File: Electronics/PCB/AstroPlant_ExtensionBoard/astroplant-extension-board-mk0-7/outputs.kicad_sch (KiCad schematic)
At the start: 17 parts, among them J12 JST-XH_LED_GND, J13 GS3, J14 GS3, J15 GS3, J16 JST_HX_2, J17 JST_HX_2, J18 JST_HX_2, J19 JST_HX_2, Q3 IRLML6344TRPBF, Q4 IRLML6344TRPBF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

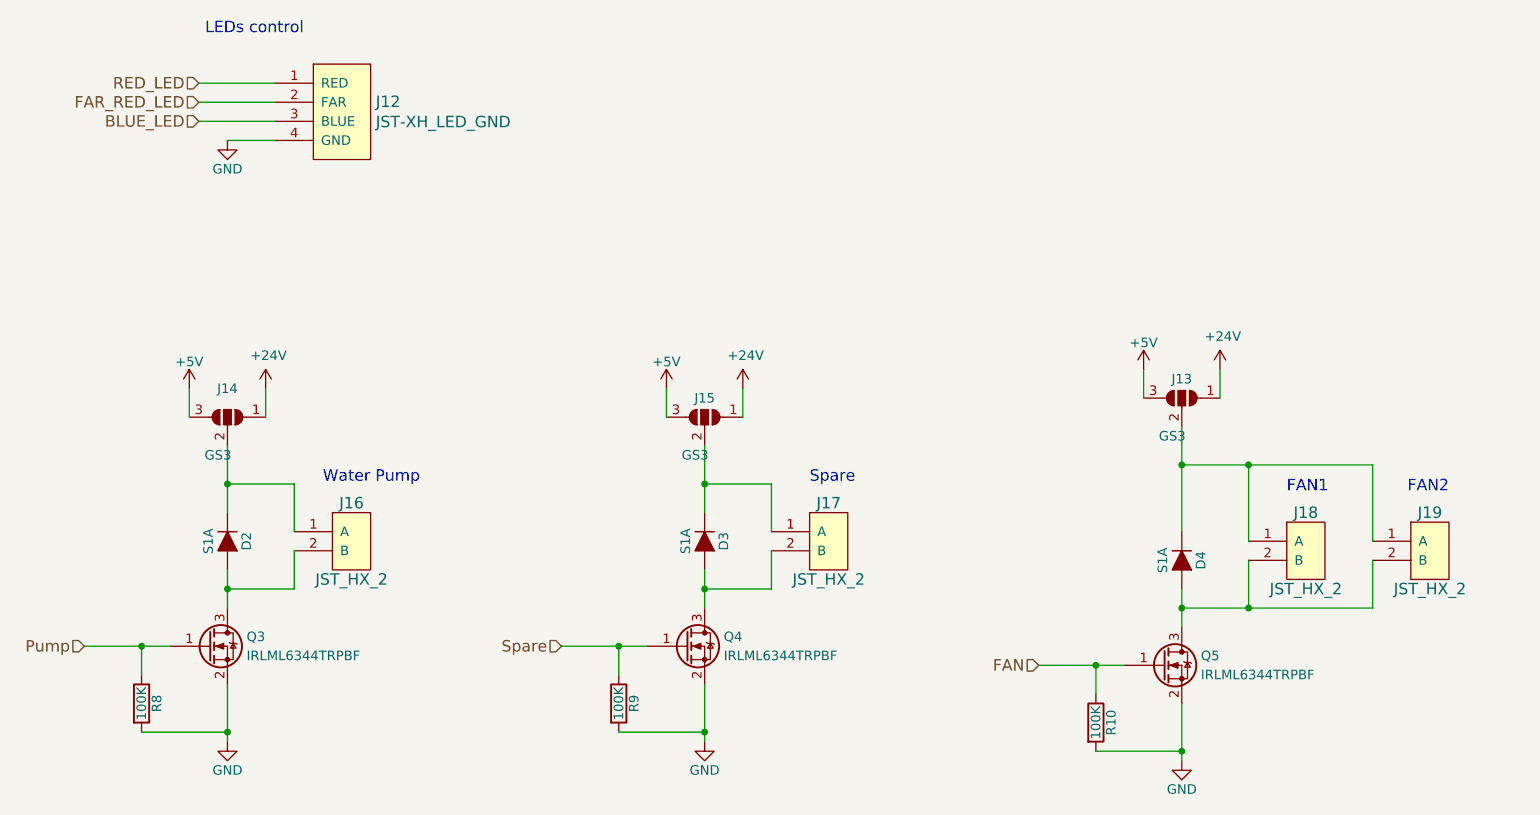
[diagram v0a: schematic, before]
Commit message: Update schematic and change library path
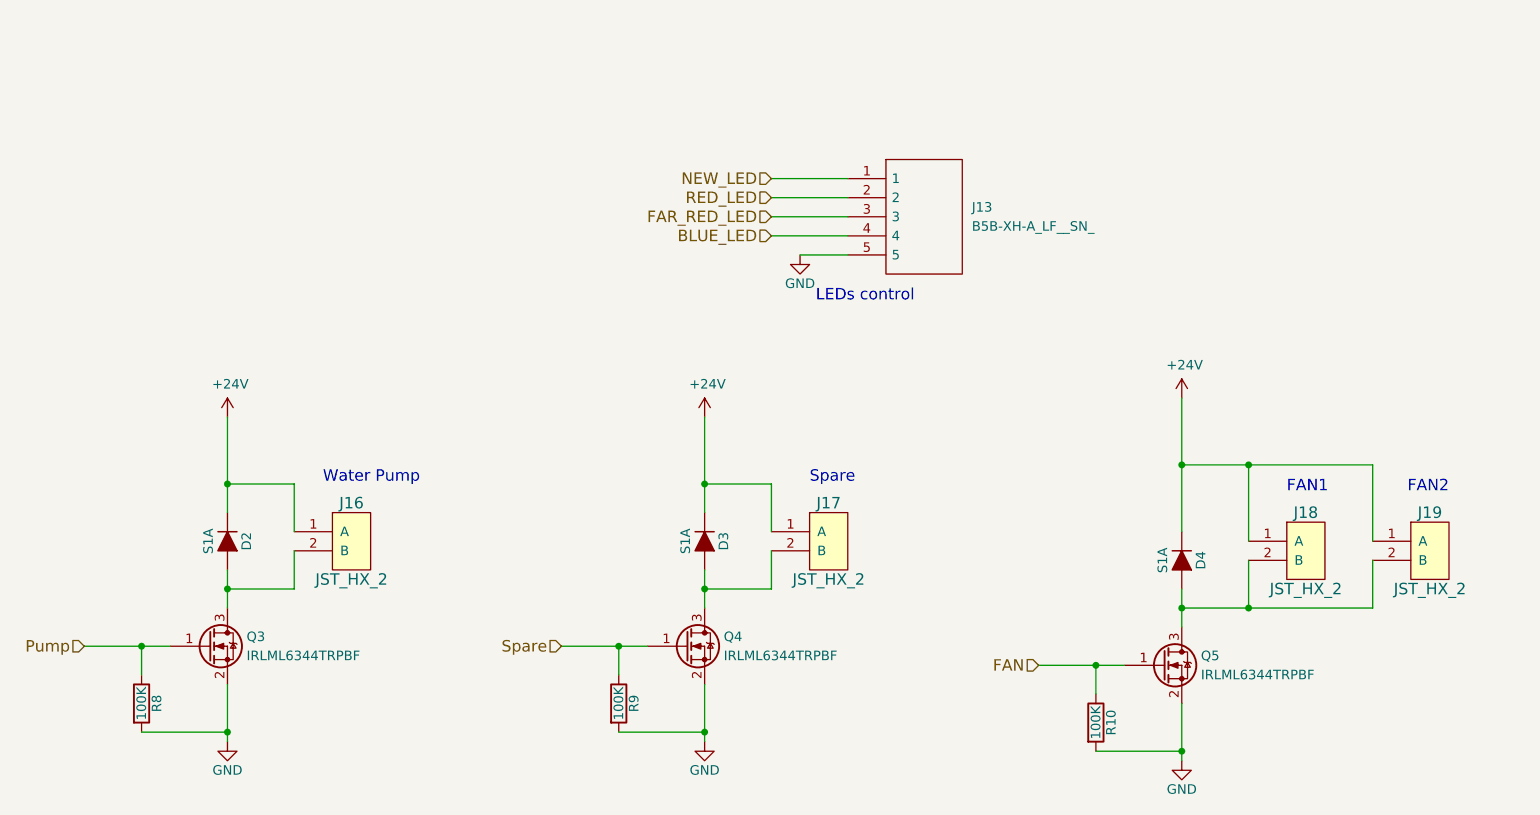
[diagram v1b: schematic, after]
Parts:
- removed J12: JST-XH_LED_GND, Connector_JST:JST_XH_B04B-XH-A_1x04_P2.50mm_Vertical, symbol Astroplant_VFR-rescue:JST-XH_LED_GND-JST_connector
- removed J13, J14, J15: GS3, Jumper:SolderJumper-3_P2.0mm_Open_TrianglePad1.0x1.5mm, symbol Astroplant_VFR-rescue:SolderJumper_3_Open-Jumper
- added J13: B5B-XH-A_LF__SN_, SHDR5W64P0X250_1X5_1490X575X700P, symbol SamacSys_Parts:B5B-XH-A_LF__SN_
- J16, J17, J18, J19: footprint Connector_JST:JST_XH_B02B-XH-A_1x02_P2.50mm_Vertical -> SamacSys_Parts:SHDR2W64P0X250_1X2_740X575X700P
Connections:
- net +24V: now also D2.1 (K), D3.1 (K), D4.1 (K), J16.1 (A), J17.1 (A), J18.1 (A), J19.1 (A)
- net BLUE_LED: now also J13.4
- net FAR_RED_LED: now also J13.3
- net GND: now also J13.5
- net RED_LED: now also J13.2
- new net NEW_LED: J13.1

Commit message: Place components on PCB
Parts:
- removed R10, R8, R9: 100K, Resistor_SMD:R_0805_2012Metric, symbol Device:R
- added R24, R25 (x2): 10k, Resistor_SMD:R_0603_1608Metric, symbol Device:R_Small
- J13: footprint SHDR5W64P0X250_1X5_1490X575X700P -> SamacSys_Parts:SHDR5W64P0X250_1X5_1490X575X700P
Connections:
- net FAN: now also R25.2
- net GND: now also R24.1, R25.1, R25.1
- net Pump: now also R24.2
- net Spare: now also R25.2
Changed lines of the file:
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@@
+    (stroke (width 0) (type default))
+  )
+  (wire (pts (xy 121.92 135.89) (xy 121.92 138.43))
     (stroke (width 0) (type default))
   )
@@
     (stroke (width 0) (type default))
   )
+  (wire (pts (xy 58.42 135.89) (xy 58.42 138.43))
+    (stroke (width 0) (type default))
+  )
   (wire (pts (xy 69.85 96.52) (xy 69.85 105.41))
     (stroke (width 0) (type default))
@@
   )
   (wire (pts (xy 205.74 113.03) (xy 205.74 102.87))
+    (stroke (width 0) (type default))
+  )
+  (wire (pts (xy 185.42 138.43) (xy 185.42 140.97))
     (stroke (width 0) (type default))
   )
@@
         (path "/51acab52-3cd6-4bba-9dee-c12efd332038/00000000-0000-0000-0000-00005a604cdc"
           (reference "D4") (unit 1)
-        )
-      )
-    )
-  )
-  (symbol (lib_id "Device:R") (at 58.42 134.62 0) (unit 1)
-    (in_bom yes) (on_board yes) (dnp no)
-    (property "Reference" "R8" (at 60.452 134.62 90)
-      (effects (font (size 1.27 1.27)))
-    )
-    (property "Value" "100K" (at 58.42 134.62 90)
-      (effects (font (size 1.27 1.27)))
-    )
-    (property "Footprint" "Resistor_SMD:R_0805_2012Metric" (at 56.642 134.62 90)
-      (effects (font (size 1.27 1.27)) hide)
-    )
-    (property "Datasheet" "http://www.yageo.com/documents/recent/PYu-RC_Group_51_RoHS_L_8.pdf" (at 58.42 134.62 0)
-      (effects (font (size 1.27 1.27)) hide)
-    )
-    (property "MPN" "RC0805FR-07100KL " (at 58.42 134.62 0)
-      (effects (font (size 1.524 1.524)) hide)
-    )
-    (property "URL" "https://www.digikey.com/product-detail/en/yageo/RC0805FR-07100KL/311-100KCRCT-ND/730491" (at 58.42 134.62 0)
-      (effects (font (size 1.524 1.524)) hide)
-    )
-    (property "Digikey Part Number" "311-100KCRCT-ND" (at 58.42 134.62 0)
-      (effects (font (size 1.524 1.524)) hide)
-    )
-    (pin "1")
-    (pin "2")
-    (instances
-      (project "Astroplant_VFR"
-        (path "/4e818498-015c-45b7-982b-80c19490efdc/00000000-0000-0000-0000-00005a604cdc"
-          (reference "R8") (unit 1)
-        )
-      )
-      (project "Astroplant_AL"
-        (path "/51acab52-3cd6-4bba-9dee-c12efd332038/00000000-0000-0000-0000-00005a604cdc"
-          (reference "R8") (unit 1)
-        )
-      )
-    )
-  )
-  (symbol (lib_id "Device:R") (at 185.42 137.16 0) (unit 1)
-    (in_bom yes) (on_board yes) (dnp no)
-    (property "Reference" "R10" (at 187.452 137.16 90)
-      (effects (font (size 1.27 1.27)))
-    )
-    (property "Value" "100K" (at 185.42 137.16 90)
-      (effects (font (size 1.27 1.27)))
-    )
-    (property "Footprint" "Resistor_SMD:R_0805_2012Metric" (at 183.642 137.16 90)
-      (effects (font (size 1.27 1.27)) hide)
-    )
-    (property "Datasheet" "http://www.yageo.com/documents/recent/PYu-RC_Group_51_RoHS_L_8.pdf" (at 185.42 137.16 0)
-      (effects (font (size 1.27 1.27)) hide)
-    )
-    (property "MPN" "RC0805FR-07100KL " (at 185.42 137.16 0)
-      (effects (font (size 1.524 1.524)) hide)
-    )
-    (property "URL" "https://www.digikey.com/product-detail/en/yageo/RC0805FR-07100KL/311-100KCRCT-ND/730491" (at 185.42 137.16 0)
-      (effects (font (size 1.524 1.524)) hide)
-    )
-    (property "Digikey Part Number" "311-100KCRCT-ND" (at 185.42 137.16 0)
-      (effects (font (size 1.524 1.524)) hide)
-    )
-    (pin "1")
-    (pin "2")
-    (instances
-      (project "Astroplant_VFR"
-        (path "/4e818498-015c-45b7-982b-80c19490efdc/00000000-0000-0000-0000-00005a604cdc"
-          (reference "R10") (unit 1)
-        )
-      )
-      (project "Astroplant_AL"
-        (path "/51acab52-3cd6-4bba-9dee-c12efd332038/00000000-0000-0000-0000-00005a604cdc"
-          (reference "R10") (unit 1)
-        )
-      )
-    )
-  )
-  (symbol (lib_id "Device:R") (at 121.92 134.62 0) (unit 1)
-    (in_bom yes) (on_board yes) (dnp no)
-    (property "Reference" "R9" (at 123.952 134.62 90)
-      (effects (font (size 1.27 1.27)))
-    )
-    (property "Value" "100K" (at 121.92 134.62 90)
-      (effects (font (size 1.27 1.27)))
-    )
-    (property "Footprint" "Resistor_SMD:R_0805_2012Metric" (at 120.142 134.62 90)
-      (effects (font (size 1.27 1.27)) hide)
-    )
-    (property "Datasheet" "http://www.yageo.com/documents/recent/PYu-RC_Group_51_RoHS_L_8.pdf" (at 121.92 134.62 0)
-      (effects (font (size 1.27 1.27)) hide)
-    )
-    (property "MPN" "RC0805FR-07100KL " (at 121.92 134.62 0)
-      (effects (font (size 1.524 1.524)) hide)
-    )
-    (property "URL" "https://www.digikey.com/product-detail/en/yageo/RC0805FR-07100KL/311-100KCRCT-ND/730491" (at 121.92 134.62 0)
-      (effects (font (size 1.524 1.524)) hide)
-    )
-    (property "Digikey Part Number" "311-100KCRCT-ND" (at 121.92 134.62 0)
-      (effects (font (size 1.524 1.524)) hide)
-    )
-    (pin "1")
-    (pin "2")
-    (instances
-      (project "Astroplant_VFR"
-        (path "/4e818498-015c-45b7-982b-80c19490efdc/00000000-0000-0000-0000-00005a604cdc"
-          (reference "R9") (unit 1)
-        )
-      )
-      (project "Astroplant_AL"
-        (path "/51acab52-3cd6-4bba-9dee-c12efd332038/00000000-0000-0000-0000-00005a604cdc"
-          (reference "R9") (unit 1)
         )
       )
@@
       (effects (font (size 1.27 1.27)) (justify left))
     )
-    (property "Footprint" "SHDR5W64P0X250_1X5_1490X575X700P" (at 168.91 62.23 0)
+    (property "Footprint" "SamacSys_Parts:SHDR5W64P0X250_1X5_1490X575X700P" (at 168.91 62.23 0)
       (effects (font (size 1.27 1.27)) (justify left) hide)
     )
@@
     )
   )
+  (symbol (lib_id "Device:R_Small") (at 185.42 135.89 180) (unit 1)
+    (in_bom yes) (on_board yes) (dnp no) (fields_autoplaced)
+    (property "Reference" "R25" (at 187.96 134.62 0)
+      (effects (font (size 1.27 1.27)) (justify right))
+    )
+    (property "Value" "10k" (at 187.96 137.16 0)
+      (effects (font (size 1.27 1.27)) (justify right))
+    )
+    (property "Footprint" "Resistor_SMD:R_0603_1608Metric" (at 185.42 135.89 0)
+      (effects (font (size 1.27 1.27)) hide)
+    )
+    (property "Datasheet" "~" (at 185.42 135.89 0)
+      (effects (font (size 1.27 1.27)) hide)
+    )
+    (property "MPN" "CRCW060310K0DHEAP" (at 185.42 135.89 0)
+      (effects (font (size 1.27 1.27)) hide)
+    )
+    (pin "1")
+    (pin "2")
+    (instances
+      (project "Astroplant_AL"
+        (path "/51acab52-3cd6-4bba-9dee-c12efd332038/5f0c961f-7fa6-4a15-8a74-755a432cc19e"
+          (reference "R25") (unit 1)
+        )
+        (path "/51acab52-3cd6-4bba-9dee-c12efd332038/00000000-0000-0000-0000-00005a604cdc"
+          (reference "R10") (unit 1)
+        )
+      )
+    )
+  )
   (symbol (lib_id "power:GND") (at 146.05 74.93 0) (unit 1)
     (in_bom yes) (on_board yes) (dnp no)
@@
         )
       )
+    )
+  )
+  (symbol (lib_id "Device:R_Small") (at 121.92 133.35 180) (unit 1)
+    (in_bom yes) (on_board yes) (dnp no) (fields_autoplaced)
+    (property "Reference" "R25" (at 124.46 132.08 0)
+      (effects (font (size 1.27 1.27)) (justify right))
+    )
+    (property "Value" "10k" (at 124.46 134.62 0)
+      (effects (font (size 1.27 1.27)) (justify right))
+    )
+    (property "Footprint" "Resistor_SMD:R_0603_1608Metric" (at 121.92 133.35 0)
+      (effects (font (size 1.27 1.27)) hide)
+    )
+    (property "Datasheet" "~" (at 121.92 133.35 0)
+      (effects (font (size 1.27 1.27)) hide)
+    )
+    (property "MPN" "CRCW060310K0DHEAP" (at 121.92 133.35 0)
+      (effects (font (size 1.27 1.27)) hide)
+    )
+    (pin "1")
+    (pin "2")
+    (instances
+      (project "Astroplant_AL"
+        (path "/51acab52-3cd6-4bba-9dee-c12efd332038/5f0c961f-7fa6-4a15-8a74-755a432cc19e"
+          (reference "R25") (unit 1)
+        )
+        (path "/51acab52-3cd6-4bba-9dee-c12efd332038/00000000-0000-0000-0000-00005a604cdc"
+          (reference "R9") (unit 1)
+        )
+      )
+    )
+  )
+  (symbol (lib_id "Device:R_Small") (at 58.42 133.35 180) (unit 1)
+    (in_bom yes) (on_board yes) (dnp no) (fields_autoplaced)
+    (property "Reference" "R24" (at 60.96 132.08 0)
+      (effects (font (size 1.27 1.27)) (justify right))
+    )
+    (property "Value" "10k" (at 60.96 134.62 0)
+      (effects (font (size 1.27 1.27)) (justify right))
+    )
+    (property "Footprint" "Resistor_SMD:R_0603_1608Metric" (at 58.42 133.35 0)
+      (effects (font (size 1.27 1.27)) hide)
+    )
+    (property "Datasheet" "~" (at 58.42 133.35 0)
+      (effects (font (size 1.27 1.27)) hide)
+    )
+    (property "MPN" "CRCW060310K0DHEAP" (at 58.42 133.35 0)
+      (effects (font (size 1.27 1.27)) hide)
+    )
+    (pin "1")
+    (pin "2")
+    (instances
+      (project "Astroplant_AL"
+        (path "/51acab52-3cd6-4bba-9dee-c12efd332038/5f0c961f-7fa6-4a15-8a74-755a432cc19e"
+          (reference "R24") (unit 1)
+        )
+        (path "/51acab52-3cd6-4bba-9dee-c12efd332038/00000000-0000-0000-0000-00005a604cdc"
+          (reference "R8") (unit 1)
+        )
+      )

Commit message: Completed version of the project
Generate outputs (BOM, Drill, Pkp, Gerber)
Added connectors descritption (like "I2C 3.3V" dor the corresponding connector)
Added a connector to an external antenna
Changed routing
Changed component placement
Added a script to generate a usable BOM
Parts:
- J13: MPN (none) -> B5B-XH-A(LF)(SN)
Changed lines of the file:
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@@
       (effects (font (size 1.27 1.27)) (justify left) hide)
+    )
+    (property "MPN" "B5B-XH-A(LF)(SN)" (at 152.4 64.77 0)
+      (effects (font (size 1.27 1.27)) hide)
     )
     (pin "1")

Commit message: Updated PCB from a backup save to solve issue with git
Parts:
- D2, D3, D4: value S1A -> S1A-13-F
- J13: value B5B-XH-A_LF__SN_ -> B5B-XH-A(LF)(SN)
- J16, J17, J18, J19: value JST_HX_2 -> B2B-XH-A(LF)(SN)
- R24, R25: value 10k -> CRCW060310K0DHEAP
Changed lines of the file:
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@@
       (effects (font (size 1.27 1.27)))
     )
-    (property "Value" "S1A" (at 67.31 113.03 0)
+    (property "Value" "S1A-13-F" (at 67.31 113.03 0)
       (effects (font (size 1.27 1.27)))
     )
@@
       (effects (font (size 1.27 1.27)))
     )
-    (property "Value" "S1A" (at 130.81 113.03 0)
+    (property "Value" "S1A-13-F" (at 130.81 113.03 0)
       (effects (font (size 1.27 1.27)))
     )
@@
       (effects (font (size 1.27 1.27)))
     )
-    (property "Value" "S1A" (at 194.31 115.57 0)
+    (property "Value" "S1A-13-F" (at 194.31 115.57 0)
       (effects (font (size 1.27 1.27)))
     )
@@
       (effects (font (size 1.524 1.524)))
     )
-    (property "Value" "JST_HX_2" (at 213.36 119.38 0)
+    (property "Value" "B2B-XH-A(LF)(SN) " (at 213.36 119.38 0)
       (effects (font (size 1.524 1.524)))
     )
@@
       (effects (font (size 1.524 1.524)))
     )
-    (property "Value" "JST_HX_2" (at 229.87 119.38 0)
+    (property "Value" "B2B-XH-A(LF)(SN) " (at 229.87 119.38 0)
       (effects (font (size 1.524 1.524)))
     )
@@
       (effects (font (size 1.524 1.524)))
     )
-    (property "Value" "JST_HX_2" (at 149.86 118.11 0)
+    (property "Value" "B2B-XH-A(LF)(SN) " (at 149.86 118.11 0)
       (effects (font (size 1.524 1.524)))
     )
@@
       (effects (font (size 1.524 1.524)))
     )
-    (property "Value" "JST_HX_2" (at 86.36 118.11 0)
+    (property "Value" "B2B-XH-A(LF)(SN) " (at 86.36 118.11 0)
       (effects (font (size 1.524 1.524)))
     )
@@
       (effects (font (size 1.27 1.27)) (justify left))
     )
-    (property "Value" "B5B-XH-A_LF__SN_" (at 168.91 71.12 0)
+    (property "Value" "B5B-XH-A(LF)(SN)" (at 168.91 71.12 0)
       (effects (font (size 1.27 1.27)) (justify left))
     )
@@
       (effects (font (size 1.27 1.27)) (justify right))
     )
-    (property "Value" "10k" (at 187.96 137.16 0)
+    (property "Value" "CRCW060310K0DHEAP" (at 187.96 137.16 0)
       (effects (font (size 1.27 1.27)) (justify right))
     )
@@
       (effects (font (size 1.27 1.27)) (justify right))
     )
-    (property "Value" "10k" (at 124.46 134.62 0)
+    (property "Value" "CRCW060310K0DHEAP" (at 124.46 134.62 0)
       (effects (font (size 1.27 1.27)) (justify right))
     )
@@
       (effects (font (size 1.27 1.27)) (justify right))
     )
-    (property "Value" "10k" (at 60.96 134.62 0)
+    (property "Value" "CRCW060310K0DHEAP" (at 60.96 134.62 0)
       (effects (font (size 1.27 1.27)) (justify right))
     )

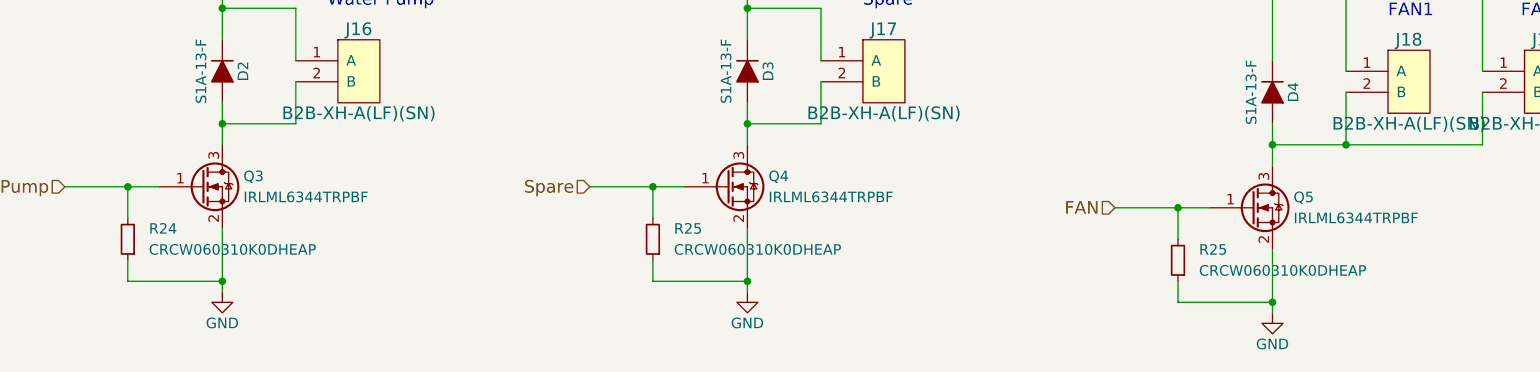
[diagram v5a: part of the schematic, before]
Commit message: Last commit (software + hardware change)
hardware : updated readme, change pcb to solve the issues of the 1st prototype
software : add code (to create a zigbee network)
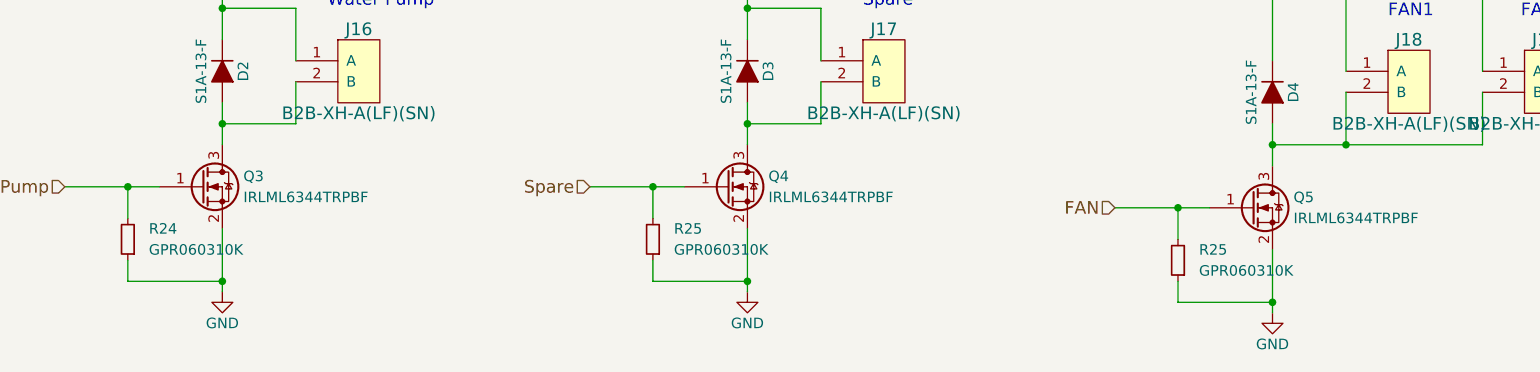
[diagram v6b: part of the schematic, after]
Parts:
- R24, R25: value CRCW060310K0DHEAP -> GPR060310K; MPN CRCW060310K0DHEAP -> GPR060310K
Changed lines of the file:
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@@
       (effects (font (size 1.27 1.27)) (justify right))
     )
-    (property "Value" "CRCW060310K0DHEAP" (at 187.96 137.16 0)
+    (property "Value" "GPR060310K" (at 187.96 137.16 0)
       (effects (font (size 1.27 1.27)) (justify right))
     )
@@
       (effects (font (size 1.27 1.27)) hide)
     )
-    (property "MPN" "CRCW060310K0DHEAP" (at 185.42 135.89 0)
+    (property "MPN" "GPR060310K" (at 185.42 135.89 0)
       (effects (font (size 1.27 1.27)) hide)
     )
@@
       (effects (font (size 1.27 1.27)) (justify right))
     )
-    (property "Value" "CRCW060310K0DHEAP" (at 124.46 134.62 0)
+    (property "Value" "GPR060310K" (at 124.46 134.62 0)
       (effects (font (size 1.27 1.27)) (justify right))
     )
@@
       (effects (font (size 1.27 1.27)) hide)
     )
-    (property "MPN" "CRCW060310K0DHEAP" (at 121.92 133.35 0)
+    (property "MPN" "GPR060310K" (at 121.92 133.35 0)
       (effects (font (size 1.27 1.27)) hide)
     )
@@
       (effects (font (size 1.27 1.27)) (justify right))
     )
-    (property "Value" "CRCW060310K0DHEAP" (at 60.96 134.62 0)
+    (property "Value" "GPR060310K" (at 60.96 134.62 0)
       (effects (font (size 1.27 1.27)) (justify right))
     )
@@
       (effects (font (size 1.27 1.27)) hide)
     )
-    (property "MPN" "CRCW060310K0DHEAP" (at 58.42 133.35 0)
+    (property "MPN" "GPR060310K" (at 58.42 133.35 0)
       (effects (font (size 1.27 1.27)) hide)
     )
